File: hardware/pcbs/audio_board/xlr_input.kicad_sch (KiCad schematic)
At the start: 24 parts, among them J6 NC3FAH1, Q2 2N7002, Q3 SI2309CDS-T1-GE3

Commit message: prepare for clock fanout
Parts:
- removed R25: 2.2kΩ, Resistor_SMD:R_0805_2012Metric, symbol Device:R
- added R33: 10Ω, Resistor_SMD:R_0805_2012Metric, symbol Device:R
- R34: renamed from R26; value 2.2kΩ -> 10Ω; MPN R 2.2kΩ 125mW 1% 0805 -> R 10Ω 125mW 1% 0805
- R36: renamed from R28; now not fitted
- renumbered R19 to R27, R20 to R28, R21 to R29, R22 to R30, R23 to R31, R24 to R32, R27 to R35, R29 to R37, R30 to R38
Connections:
- net at L5.2, R30.2: now also R33.1
- net at C42.2, C43.1, R36.1: now also R33.2
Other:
- note added: "for ≈6dB pad with ≈10kΩ impedance use 2.2kΩ series resistors and 13kΩ parallel resistor"
- note removed: "replace with 10Ω and remove parallel resistor to disable pad"
- note removed: "≈6dB pad with ≈10k impedance"

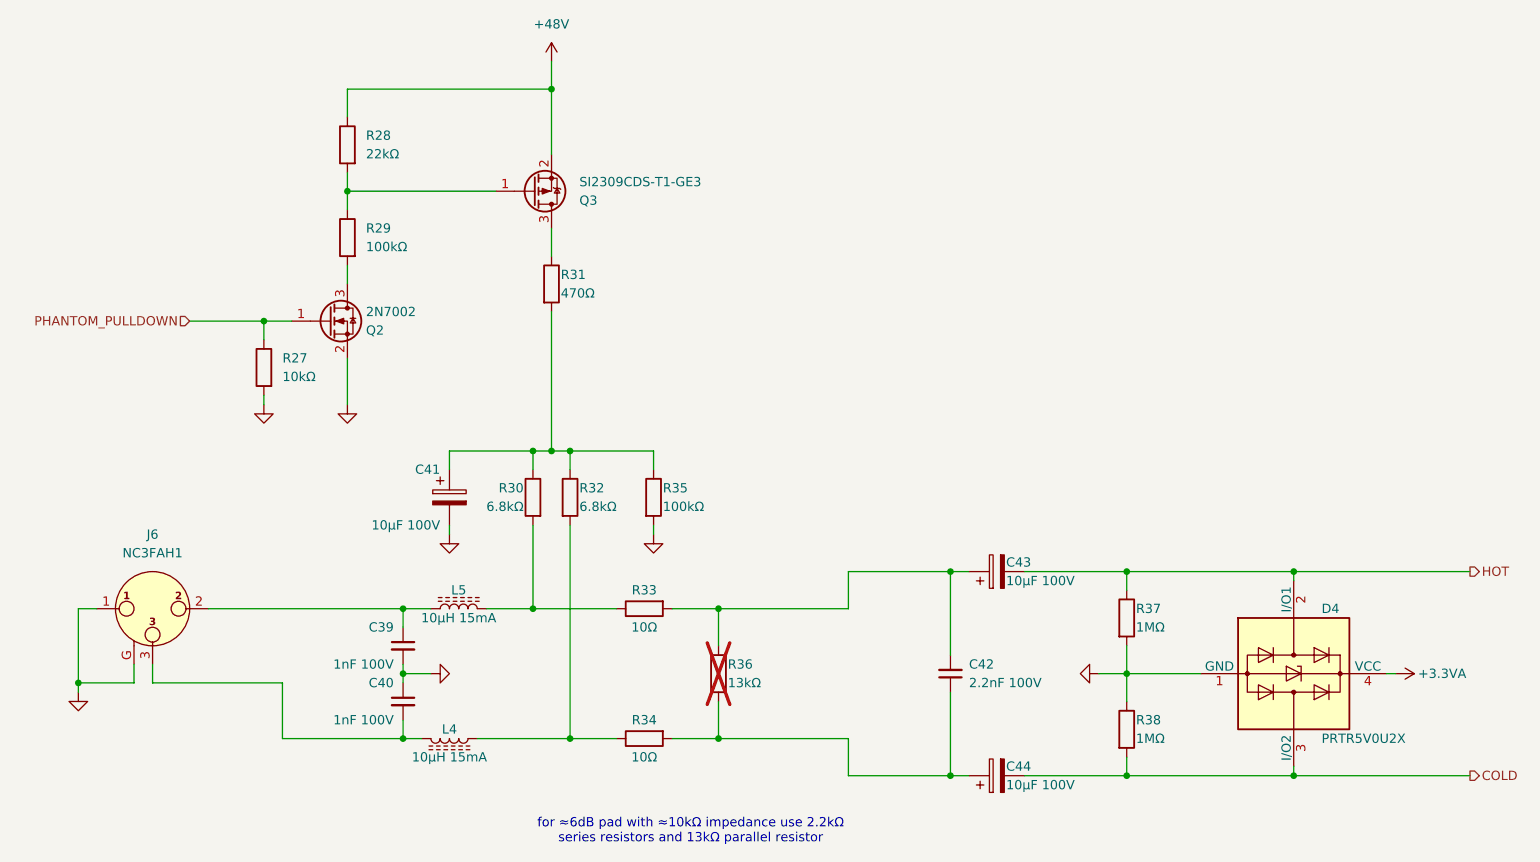
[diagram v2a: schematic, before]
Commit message: audioboard: route clock fanout
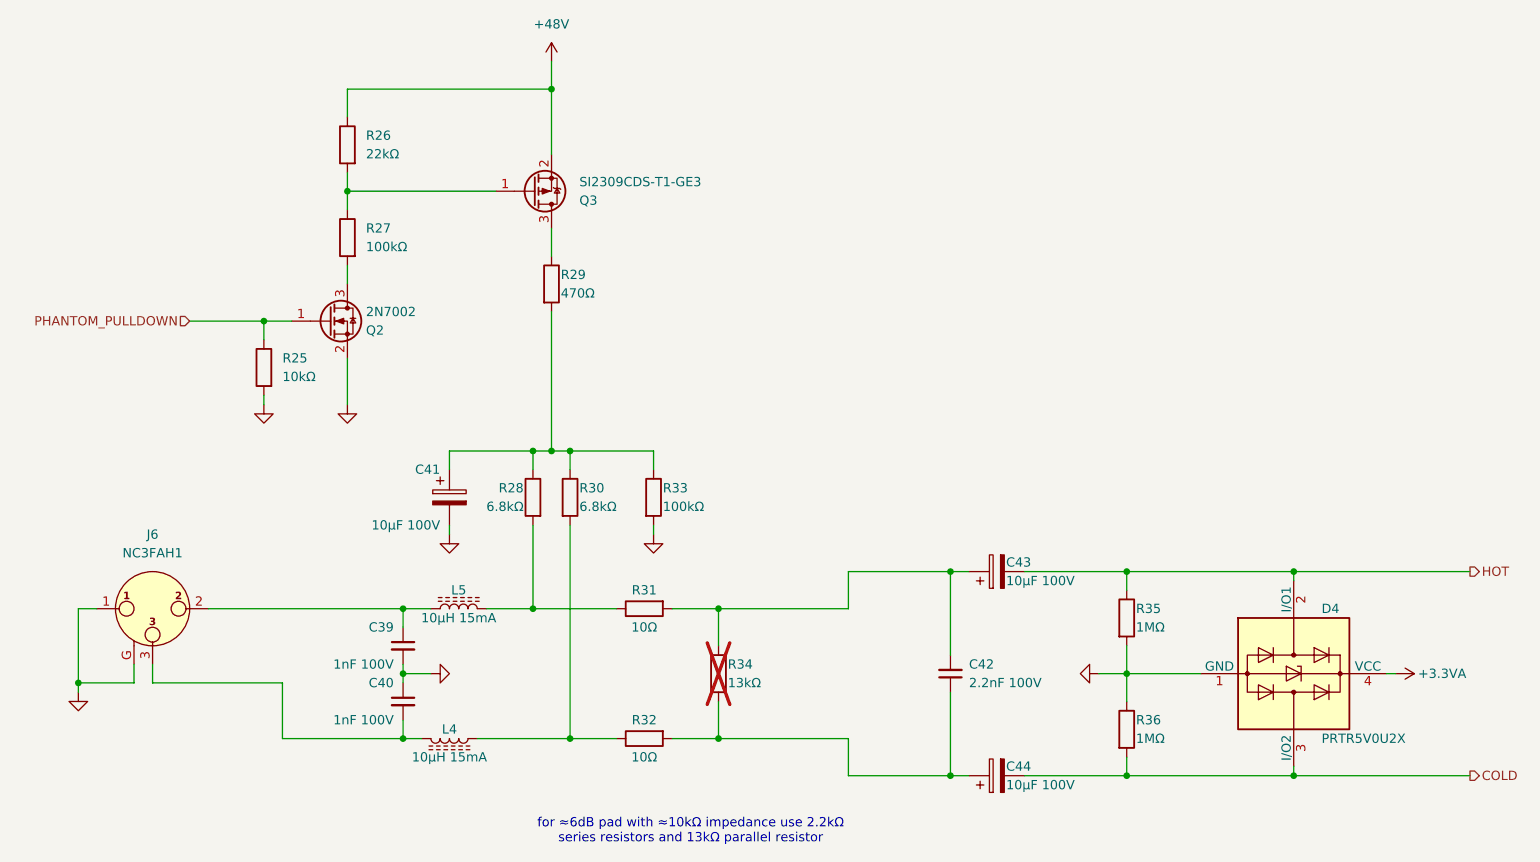
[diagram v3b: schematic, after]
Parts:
- renumbered R27 to R25, R28 to R26, R29 to R27, R30 to R28, R31 to R29, R32 to R30, R33 to R31, R34 to R32, R35 to R33, R36 to R34, R37 to R35, R38 to R36
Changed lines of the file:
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@@
 		(in_pos_files yes)
 		(dnp no)
-		(property "Reference" "R34"
+		(property "Reference" "R32"
 			(at 113.03 120.65 90)
 			(show_name no)
@@
 			(project "audio_board"
 				(path "/54443f96-c7c5-4432-b890-45b14a1547a1/8957bb4e-7be5-4513-a482-a60a2150a7cb"
-					(reference "R58")
+					(reference "R56")
 					(unit 1)
 				)
 				(path "/54443f96-c7c5-4432-b890-45b14a1547a1/91e2e940-fc71-4db8-9476-c8ec62bf0617"
-					(reference "R46")
+					(reference "R44")
 					(unit 1)
 				)
 				(path "/54443f96-c7c5-4432-b890-45b14a1547a1/b0f2da11-13c7-4314-8470-ff6d99797a55"
-					(reference "R34")
+					(reference "R32")
 					(unit 1)
 				)
@@
 		(in_pos_files yes)
 		(dnp no)
-		(property "Reference" "R32"
+		(property "Reference" "R30"
 			(at 104.14 88.9 0)
 			(show_name no)
@@
 			(project "audio_board"
 				(path "/54443f96-c7c5-4432-b890-45b14a1547a1/8957bb4e-7be5-4513-a482-a60a2150a7cb"
-					(reference "R56")
+					(reference "R54")
 					(unit 1)
 				)
 				(path "/54443f96-c7c5-4432-b890-45b14a1547a1/91e2e940-fc71-4db8-9476-c8ec62bf0617"
-					(reference "R44")
+					(reference "R42")
 					(unit 1)
 				)
 				(path "/54443f96-c7c5-4432-b890-45b14a1547a1/b0f2da11-13c7-4314-8470-ff6d99797a55"
-					(reference "R32")
+					(reference "R30")
 					(unit 1)
 				)
@@
 		(in_pos_files yes)
 		(dnp no)
-		(property "Reference" "R37"
+		(property "Reference" "R35"
 			(at 180.34 105.41 0)
 			(show_name no)
@@
 			(project "audio_board"
 				(path "/54443f96-c7c5-4432-b890-45b14a1547a1/8957bb4e-7be5-4513-a482-a60a2150a7cb"
-					(reference "R61")
+					(reference "R59")
 					(unit 1)
 				)
 				(path "/54443f96-c7c5-4432-b890-45b14a1547a1/91e2e940-fc71-4db8-9476-c8ec62bf0617"
-					(reference "R49")
+					(reference "R47")
 					(unit 1)
 				)
 				(path "/54443f96-c7c5-4432-b890-45b14a1547a1/b0f2da11-13c7-4314-8470-ff6d99797a55"
-					(reference "R37")
+					(reference "R35")
 					(unit 1)
 				)
@@
 		(dnp no)
 		(fields_autoplaced yes)
-		(property "Reference" "R29"
+		(property "Reference" "R27"
 			(at 74.93 53.3399 0)
 			(show_name no)
@@
 			(project "audio_board"
 				(path "/54443f96-c7c5-4432-b890-45b14a1547a1/8957bb4e-7be5-4513-a482-a60a2150a7cb"
-					(reference "R53")
+					(reference "R51")
 					(unit 1)
 				)
 				(path "/54443f96-c7c5-4432-b890-45b14a1547a1/91e2e940-fc71-4db8-9476-c8ec62bf0617"
-					(reference "R41")
+					(reference "R39")
 					(unit 1)
 				)
 				(path "/54443f96-c7c5-4432-b890-45b14a1547a1/b0f2da11-13c7-4314-8470-ff6d99797a55"
-					(reference "R29")
+					(reference "R27")
 					(unit 1)
 				)
@@
 		(in_pos_files yes)
 		(dnp no)
-		(property "Reference" "R33"
+		(property "Reference" "R31"
 			(at 113.03 102.87 90)
 			(show_name no)
@@
 			(project "audio_board"
 				(path "/54443f96-c7c5-4432-b890-45b14a1547a1/8957bb4e-7be5-4513-a482-a60a2150a7cb"
-					(reference "R57")
+					(reference "R55")
 					(unit 1)
 				)
 				(path "/54443f96-c7c5-4432-b890-45b14a1547a1/91e2e940-fc71-4db8-9476-c8ec62bf0617"
-					(reference "R45")
+					(reference "R43")
 					(unit 1)
 				)
 				(path "/54443f96-c7c5-4432-b890-45b14a1547a1/b0f2da11-13c7-4314-8470-ff6d99797a55"
-					(reference "R33")
+					(reference "R31")
 					(unit 1)
 				)
@@
 		(in_pos_files yes)
 		(dnp no)
-		(property "Reference" "R30"
+		(property "Reference" "R28"
 			(at 96.52 88.9 0)
 			(show_name no)
@@
 			(project "audio_board"
 				(path "/54443f96-c7c5-4432-b890-45b14a1547a1/8957bb4e-7be5-4513-a482-a60a2150a7cb"
-					(reference "R54")
+					(reference "R52")
 					(unit 1)
 				)
 				(path "/54443f96-c7c5-4432-b890-45b14a1547a1/91e2e940-fc71-4db8-9476-c8ec62bf0617"
-					(reference "R42")
+					(reference "R40")
 					(unit 1)
 				)
 				(path "/54443f96-c7c5-4432-b890-45b14a1547a1/b0f2da11-13c7-4314-8470-ff6d99797a55"
-					(reference "R30")
+					(reference "R28")
 					(unit 1)
 				)
@@
 		(in_pos_files yes)
 		(dnp no)
-		(property "Reference" "R35"
+		(property "Reference" "R33"
 			(at 115.57 88.9 0)
 			(show_name no)
@@
 			(project "audio_board"
 				(path "/54443f96-c7c5-4432-b890-45b14a1547a1/8957bb4e-7be5-4513-a482-a60a2150a7cb"
-					(reference "R59")
+					(reference "R57")
 					(unit 1)
 				)
 				(path "/54443f96-c7c5-4432-b890-45b14a1547a1/91e2e940-fc71-4db8-9476-c8ec62bf0617"
-					(reference "R47")
+					(reference "R45")
 					(unit 1)
 				)
 				(path "/54443f96-c7c5-4432-b890-45b14a1547a1/b0f2da11-13c7-4314-8470-ff6d99797a55"
-					(reference "R35")
+					(reference "R33")
 					(unit 1)
 				)
@@
 		(in_pos_files yes)
 		(dnp no)
-		(property "Reference" "R38"
+		(property "Reference" "R36"
 			(at 180.34 120.65 0)
 			(show_name no)
@@
 			(project "audio_board"
 				(path "/54443f96-c7c5-4432-b890-45b14a1547a1/8957bb4e-7be5-4513-a482-a60a2150a7cb"
-					(reference "R62")
+					(reference "R60")
 					(unit 1)
 				)
 				(path "/54443f96-c7c5-4432-b890-45b14a1547a1/91e2e940-fc71-4db8-9476-c8ec62bf0617"
-					(reference "R50")
+					(reference "R48")
 					(unit 1)
 				)
 				(path "/54443f96-c7c5-4432-b890-45b14a1547a1/b0f2da11-13c7-4314-8470-ff6d99797a55"
-					(reference "R38")
+					(reference "R36")
 					(unit 1)
 				)
@@
 		(dnp no)
 		(fields_autoplaced yes)
-		(property "Reference" "R28"
+		(property "Reference" "R26"
 			(at 74.93 40.6399 0)
 			(show_name no)
@@
 			(project "audio_board"
 				(path "/54443f96-c7c5-4432-b890-45b14a1547a1/8957bb4e-7be5-4513-a482-a60a2150a7cb"
-					(reference "R52")
+					(reference "R50")
 					(unit 1)
 				)
 				(path "/54443f96-c7c5-4432-b890-45b14a1547a1/91e2e940-fc71-4db8-9476-c8ec62bf0617"
-					(reference "R40")
+					(reference "R38")
 					(unit 1)
 				)
 				(path "/54443f96-c7c5-4432-b890-45b14a1547a1/b0f2da11-13c7-4314-8470-ff6d99797a55"
-					(reference "R28")
+					(reference "R26")
 					(unit 1)
 				)
@@
 		(in_pos_files yes)
 		(dnp no)
-		(property "Reference" "R31"
+		(property "Reference" "R29"
 			(at 101.6 59.69 0)
 			(show_name no)
@@
 			(project "audio_board"
 				(path "/54443f96-c7c5-4432-b890-45b14a1547a1/8957bb4e-7be5-4513-a482-a60a2150a7cb"
-					(reference "R55")
+					(reference "R53")
 					(unit 1)
 				)
 				(path "/54443f96-c7c5-4432-b890-45b14a1547a1/91e2e940-fc71-4db8-9476-c8ec62bf0617"
-					(reference "R43")
+					(reference "R41")
 					(unit 1)
 				)
 				(path "/54443f96-c7c5-4432-b890-45b14a1547a1/b0f2da11-13c7-4314-8470-ff6d99797a55"
-					(reference "R31")
+					(reference "R29")
 					(unit 1)
 				)
@@
 		(in_pos_files yes)
 		(dnp yes)
-		(property "Reference" "R36"
+		(property "Reference" "R34"
 			(at 124.46 113.03 0)
 			(show_name no)
@@
 			(project "audio_board"
 				(path "/54443f96-c7c5-4432-b890-45b14a1547a1/8957bb4e-7be5-4513-a482-a60a2150a7cb"
-					(reference "R60")
+					(reference "R58")
 					(unit 1)
 				)
 				(path "/54443f96-c7c5-4432-b890-45b14a1547a1/91e2e940-fc71-4db8-9476-c8ec62bf0617"
-					(reference "R48")
+					(reference "R46")
 					(unit 1)
 				)
 				(path "/54443f96-c7c5-4432-b890-45b14a1547a1/b0f2da11-13c7-4314-8470-ff6d99797a55"
-					(reference "R36")
+					(reference "R34")
 					(unit 1)
 				)
@@
 		(dnp no)
 		(fields_autoplaced yes)
-		(property "Reference" "R27"
+		(property "Reference" "R25"
 			(at 63.5 71.1199 0)
 			(show_name no)
@@
 			(project "audio_board"
 				(path "/54443f96-c7c5-4432-b890-45b14a1547a1/8957bb4e-7be5-4513-a482-a60a2150a7cb"
-					(reference "R51")
+					(reference "R49")
 					(unit 1)
 				)
 				(path "/54443f96-c7c5-4432-b890-45b14a1547a1/91e2e940-fc71-4db8-9476-c8ec62bf0617"
-					(reference "R39")
+					(reference "R37")
 					(unit 1)
 				)
 				(path "/54443f96-c7c5-4432-b890-45b14a1547a1/b0f2da11-13c7-4314-8470-ff6d99797a55"
-					(reference "R27")
+					(reference "R25")
 					(unit 1)
 				)

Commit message: audioboard: finalise routing
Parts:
- renumbered R25 to R27, R26 to R28, R27 to R29, R28 to R30, R29 to R31, R30 to R32, R31 to R33, R32 to R34, R33 to R35, R34 to R36, R35 to R37, R36 to R38

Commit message: minor changes to audioboard
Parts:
- renumbered R27 to R25, R28 to R26, R29 to R27, R30 to R28, R31 to R29, R32 to R30, R33 to R31, R34 to R32, R35 to R33, R36 to R34, R37 to R35, R38 to R36
